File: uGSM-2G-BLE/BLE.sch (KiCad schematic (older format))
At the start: 1 part

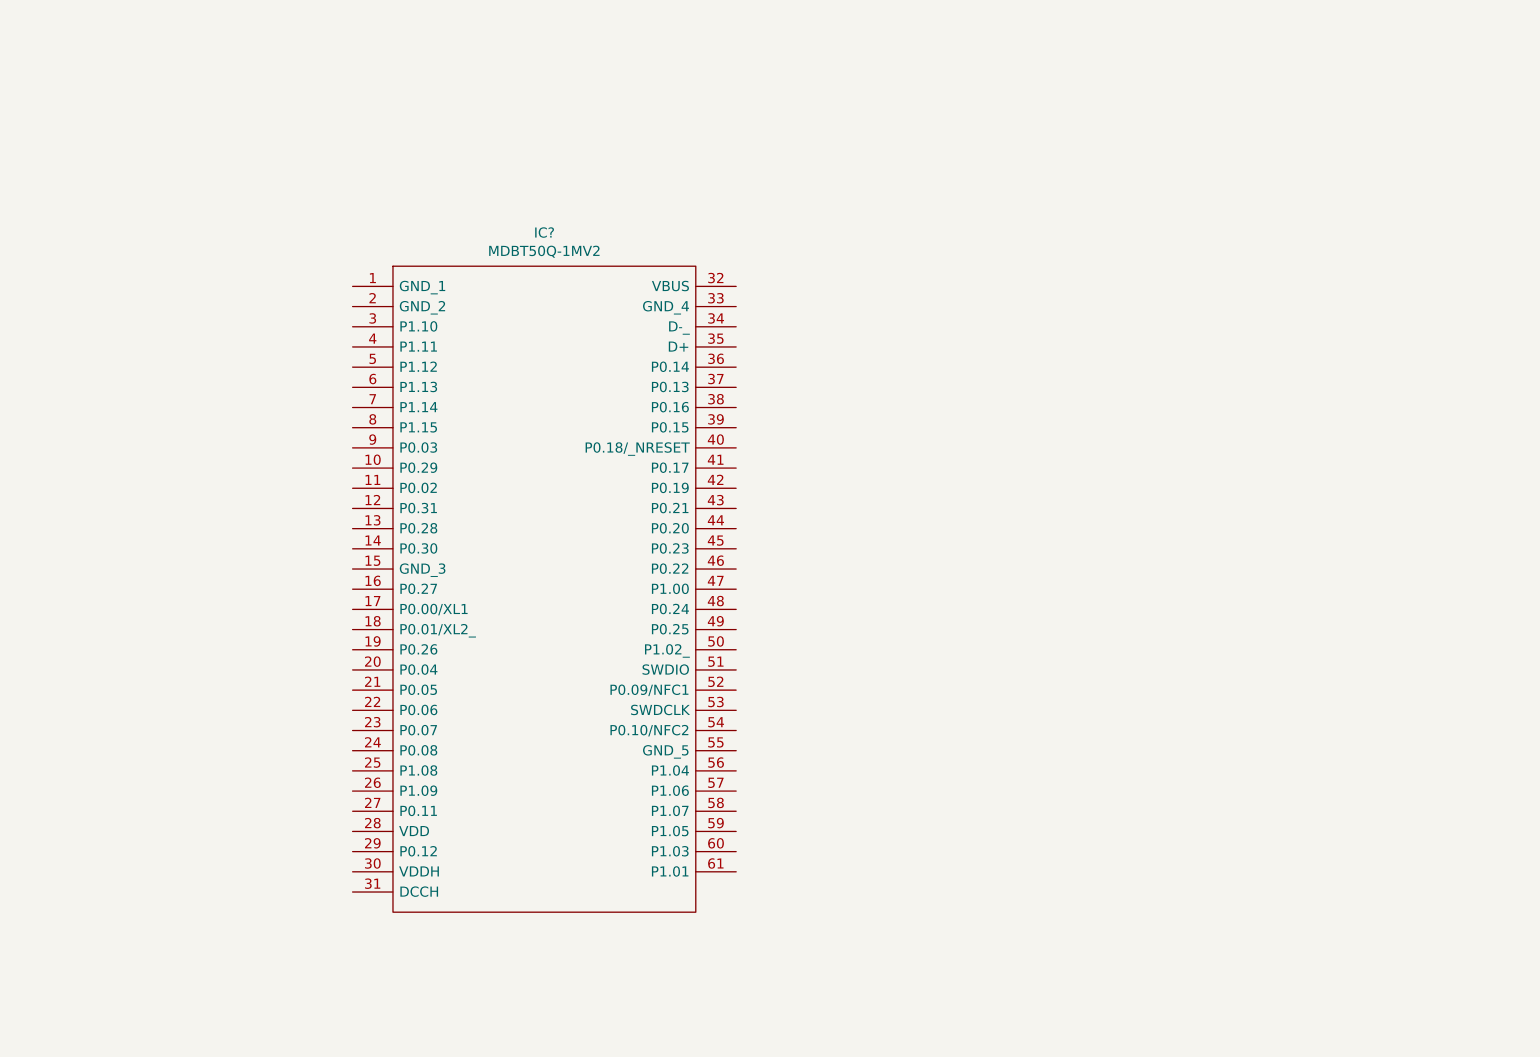
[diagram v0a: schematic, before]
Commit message: ble connected to mikrobus
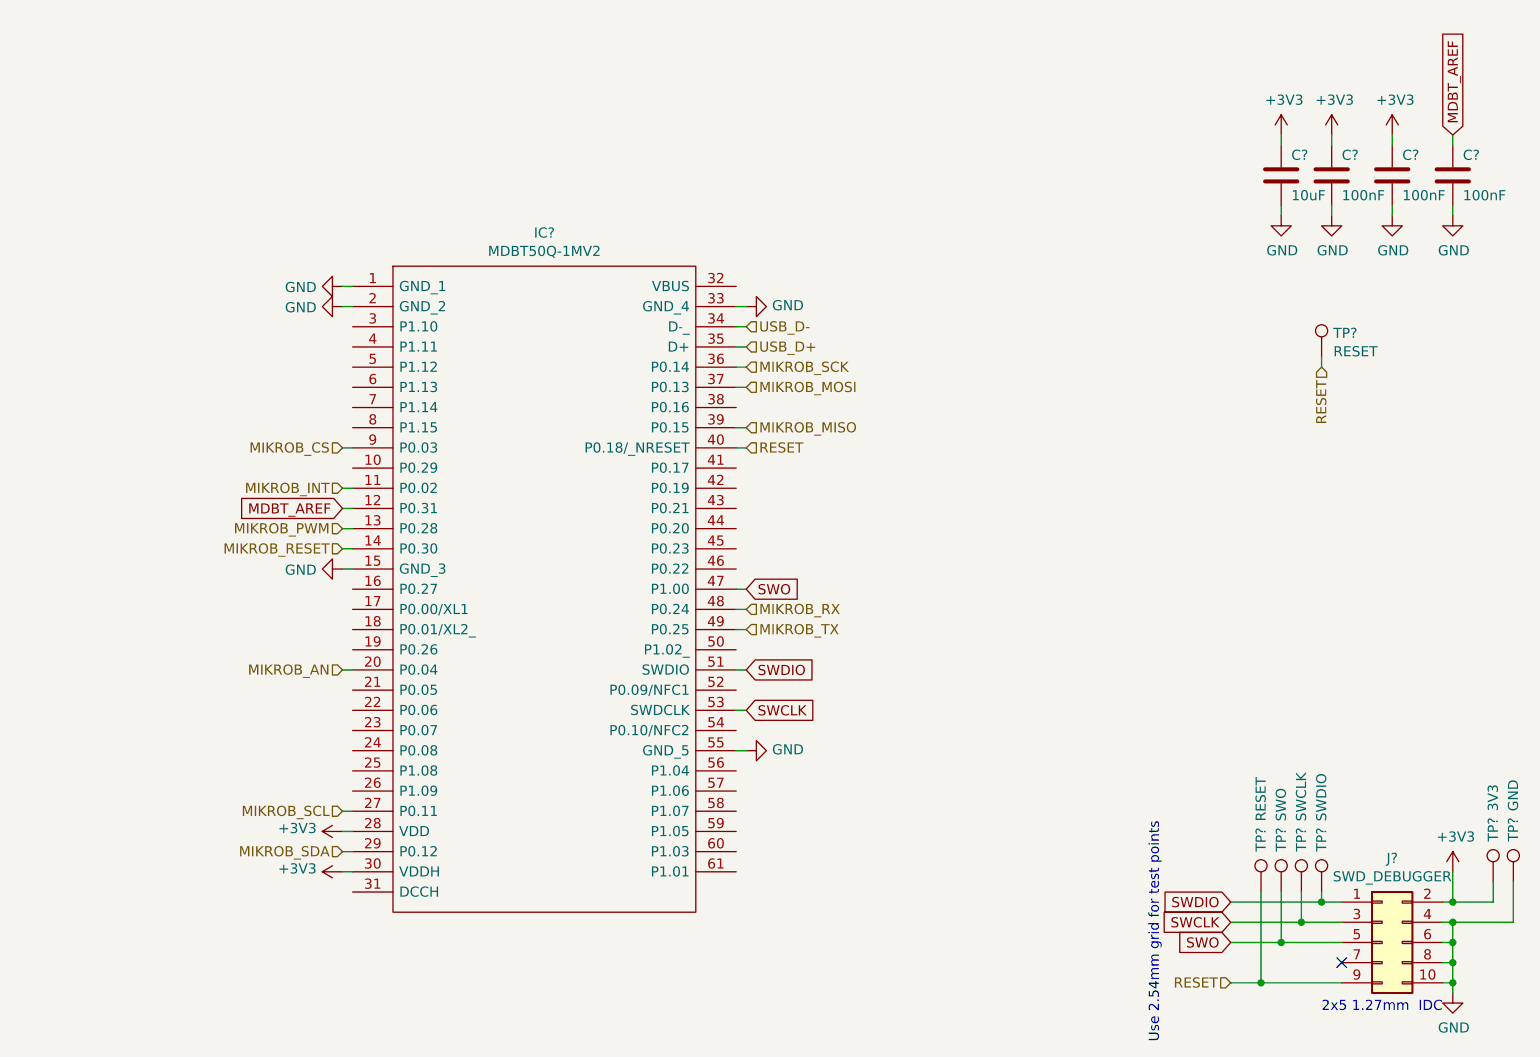
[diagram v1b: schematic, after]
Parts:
- added C?: 10uF, Capacitor_SMD:C_0603_1608Metric, symbol Device:C
- added C? (x3): 100nF, Capacitor_SMD:C_0603_1608Metric, symbol Device:C
- added J?: SWD_DEBUGGER, symbol Connector_Generic:Conn_02x05_Odd_Even
- added TP? (x2): RESET, TestPoint:TestPoint_Pad_1.0x1.0mm, symbol Connector:TestPoint
- added TP?: SWDIO, TestPoint:TestPoint_Pad_1.0x1.0mm, symbol Connector:TestPoint
- added TP?: SWCLK, TestPoint:TestPoint_Pad_1.0x1.0mm, symbol Connector:TestPoint
- added TP?: SWO, TestPoint:TestPoint_Pad_1.0x1.0mm, symbol Connector:TestPoint
- added TP?: 3V3, TestPoint:TestPoint_Pad_1.0x1.0mm, symbol Connector:TestPoint
- added TP?: GND, TestPoint:TestPoint_Pad_1.0x1.0mm, symbol Connector:TestPoint
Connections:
- net GND: now reaches IC?.1 (GND_1)
- net GND: now also IC?.15 (GND_3), IC?.2 (GND_2), IC?.33 (GND_4), IC?.55 (GND_5), C?.2, C?.2, C?.2, C?.2, J?.10 (Pin_10), J?.4 (Pin_4), J?.6 (Pin_6), J?.8 (Pin_8), TP?.1
- net MIKROB_INT: now reaches IC?.11 (P0.02)
- net MDBT_AREF: now reaches IC?.12 (P0.31)
- net MDBT_AREF: now also C?.1
- net MIKROB_PWM: now reaches IC?.13 (P0.28)
- net MIKROB_RESET: now reaches IC?.14 (P0.30)
- net MIKROB_AN: now reaches IC?.20 (P0.04)
- net MIKROB_SCL: now reaches IC?.27 (P0.11)
- net +3V3: now reaches IC?.28 (VDD)
- net +3V3: now also IC?.30 (VDDH), C?.1, C?.1, C?.1, J?.2 (Pin_2), TP?.1
- net MIKROB_SDA: now reaches IC?.29 (P0.12)
- net USB_D-: now reaches IC?.34 (D˗_)
- net USB_D+: now reaches IC?.35 (D+)
- net MIKROB_SCK: now reaches IC?.36 (P0.14)
- net MIKROB_MOSI: now reaches IC?.37 (P0.13)
- net MIKROB_MISO: now reaches IC?.39 (P0.15)
- net RESET: now reaches IC?.40 (P0.18/_NRESET)
- net RESET: now also J?.9 (Pin_9), TP?.1, TP?.1
- net SWO: now reaches IC?.47 (P1.00)
- net SWO: now also J?.5 (Pin_5), TP?.1
- net MIKROB_RX: now reaches IC?.48 (P0.24)
- net MIKROB_TX: now reaches IC?.49 (P0.25)
- net SWDIO: now reaches IC?.51 (SWDIO)
- net SWDIO: now also J?.1 (Pin_1), TP?.1
- net SWCLK: now reaches IC?.53 (SWDCLK)
- net SWCLK: now also J?.3 (Pin_3), TP?.1
- net MIKROB_CS: now reaches IC?.9 (P0.03)
- no-connect marks 0 -> 1
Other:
- note added: "2x5 1.27mm IDC"
- note added: "Use 2.54mm grid for test points\n"

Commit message: completed all issues, updating
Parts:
- added C? (x2): 22pF, Capacitor_SMD:C_0603_1608Metric, symbol Device:C
- added Y?: 32.768, symbol Device:Crystal
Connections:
- net GND: now also C?.2, C?.2
- net at IC?.17 (P0.00/XL1): now also C?.1, Y?.1
- net at IC?.18 (P0.01/XL2_): now also C?.1, Y?.2
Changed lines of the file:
@@
 Wire Wire Line
 	5000 5200 5050 5200
+$Comp
+L Device:Crystal Y?
+U 1 1 5E94CD1F
+P 4150 4250
+F 0 "Y?" V 4300 4150 50  0000 L CNN
+F 1 "32.768" H 4000 4400 50  0000 L CNN
+F 2 "" H 4150 4250 50  0001 C CNN
+F 3 "~" H 4150 4250 50  0001 C CNN
+	1    4150 4250
+	0    1    1    0
+$EndComp
+$Comp
+L Device:C C?
+U 1 1 5E94D57B
+P 3900 4050
+F 0 "C?" H 3950 4150 50  0000 L CNN
+F 1 "22pF" H 3950 3950 50  0000 L CNN
+F 2 "Capacitor_SMD:C_0603_1608Metric" H 3938 3900 50  0001 C CNN
+F 3 "~" H 3900 4050 50  0001 C CNN
+	1    3900 4050
+	0    1    1    0
+$EndComp
+$Comp
+L Device:C C?
+U 1 1 5E94DDAB
+P 3900 4450
+F 0 "C?" H 3950 4550 50  0000 L CNN
+F 1 "22pF" H 3950 4350 50  0000 L CNN
+F 2 "Capacitor_SMD:C_0603_1608Metric" H 3938 4300 50  0001 C CNN
+F 3 "~" H 3900 4450 50  0001 C CNN
+	1    3900 4450
+	0    1    1    0
+$EndComp
+Wire Wire Line
+	5050 4100 4350 4100
+Wire Wire Line
+	4350 4100 4350 4050
+Wire Wire Line
+	4350 4050 4150 4050
+Wire Wire Line
+	4150 4100 4150 4050
+Connection ~ 4150 4050
+Wire Wire Line
+	4150 4050 4050 4050
+Wire Wire Line
+	4050 4450 4150 4450
+Wire Wire Line
+	4350 4450 4350 4200
+Wire Wire Line
+	4350 4200 5050 4200
+Wire Wire Line
+	4150 4400 4150 4450
+Connection ~ 4150 4450
+Wire Wire Line
+	4150 4450 4350 4450
+Wire Wire Line
+	3750 4050 3700 4050
+Wire Wire Line
+	3750 4450 3700 4450
+$Comp
+L power:GND #PWR?
+U 1 1 5E95D9B8
+P 3700 4050
+F 0 "#PWR?" H 3700 3800 50  0001 C CNN
+F 1 "GND" V 3705 3922 50  0000 R CNN
+F 2 "" H 3700 4050 50  0001 C CNN
+F 3 "" H 3700 4050 50  0001 C CNN
+	1    3700 4050
+	0    1    1    0
+$EndComp
+$Comp
+L power:GND #PWR?
+U 1 1 5E95DC97
+P 3700 4450
+F 0 "#PWR?" H 3700 4200 50  0001 C CNN
+F 1 "GND" V 3705 4322 50  0000 R CNN
+F 2 "" H 3700 4450 50  0001 C CNN
+F 3 "" H 3700 4450 50  0001 C CNN
+	1    3700 4450
+	0    1    1    0
+$EndComp
 $EndSCHEMATC

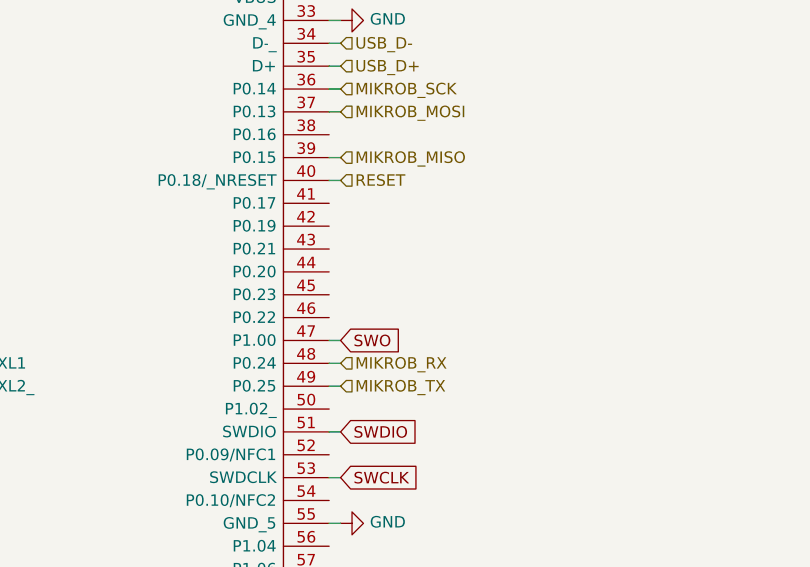
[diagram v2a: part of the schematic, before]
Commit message: removed usbl6 simcom
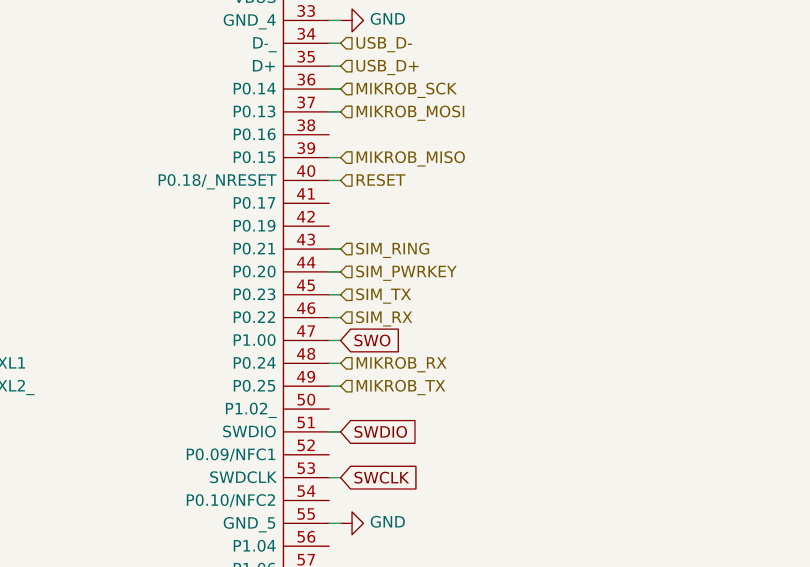
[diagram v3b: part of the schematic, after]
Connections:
- net SIM_RING: now reaches IC?.43 (P0.21)
- net SIM_PWRKEY: now reaches IC?.44 (P0.20)
- net SIM_TX: now reaches IC?.45 (P0.23)
- net SIM_RX: now reaches IC?.46 (P0.22)
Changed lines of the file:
@@
 	0    1    1    0
 $EndComp
+Text HLabel 7000 3900 2    50   Input ~ 0
+SIM_RX
+Text HLabel 7000 3800 2    50   Input ~ 0
+SIM_TX
+Wire Wire Line
+	7000 3800 6950 3800
+Wire Wire Line
+	6950 3900 7000 3900
+Text HLabel 7000 3700 2    50   Input ~ 0
+SIM_PWRKEY
+Wire Wire Line
+	6950 3700 7000 3700
+Text HLabel 7000 3600 2    50   Input ~ 0
+SIM_RING
+Wire Wire Line
+	6950 3600 7000 3600
 $EndSCHEMATC
